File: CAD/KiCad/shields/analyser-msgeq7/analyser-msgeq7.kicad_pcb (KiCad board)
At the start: 2 copper layers, 150 x 55 mm, 59 parts, among them U1 MSGEQ7N, U2 MSGEQ7N, U3 MSGEQ7N, U4 MSGEQ7N, U5 MSGEQ7N

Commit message: Remove shield identification and adopt the simplified connector and Teensy pin maps
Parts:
- removed CID1: 100nF, Shields:C_0603_1608Metric
- removed JSID1: WRITE ENABLE - OPEN, Shields:SolderJumper-2_P1.3mm_Open_RoundedPad1.0x1.5mm
- removed RID1: 10K, Shields:R_0603_1608Metric
- removed UID1: M24C02-RMN6TP, Shields:SOIC-8_3.9x4.9mm_P1.27mm
- added TPG: AGND, Shields:TestPoint_Pad_D1.5mm, F.Cu at (183.0, 90.0)
- added TPI: IOREF, Shields:TestPoint_Pad_D1.5mm, F.Cu at (178.0, 90.0)
- JA1: value ANALYSER - KEY 24 -> ANALYSER - KEY 22; footprint Shields:Socket_2x12_Key24 -> Shields:Socket_2x11_Key22
- TP11: value test pad -> male1/analyser out
- TP12: value test pad -> male2/analyser out
- TP13: value test pad -> female1/analyser out
- TP14: value test pad -> female2/analyser out
- TP15: value test pad -> female3/analyser out
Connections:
- JA1 pad 19: shield/sda -> IOREF
- JA1 pad 20: shield/scl -> (no net)
- JA1 pad 21: IOREF -> (no net)
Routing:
- net GND: track 144.2 -> 0.00 mm, vias 2 -> 0
- net shield/scl: track 140.6 -> 0.00 mm, vias 1 -> 0
- net shield/sda: track 135.4 -> 0.00 mm, vias 2 -> 0
- net IOREF: track 217.2 -> 186.1 mm, vias 4 -> 3
- net AGND: track 345.4 -> 316.4 mm, vias 10 -> 12
- net female1/analyser out: track 26.0 -> 51.6 mm, vias 2 -> 3
- net id/wp: track 19.2 -> 0.00 mm, vias 2 -> 0
- net male2/microphone: track 148.9 -> 131.6 mm, vias 1 -> 2
- net male2/analyser out: track 124.9 -> 138.0 mm, vias 2 -> 3
- net analyser/reset: track 145.6 -> 157.3 mm, vias 7 -> 6
- net female2/microphone: track 56.3 -> 66.6 mm
- net female3/microphone: track 88.5 -> 81.4 mm, vias 1 -> 2
- net male1/microphone: track 106.9 -> 113.6 mm, vias 2 -> 1
- net analyser/strobe: track 158.1 -> 164.7 mm, vias 5 -> 7
- net female2/analyser out: track 52.8 -> 46.9 mm
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- removed copper zone on B.Cu, net AGND
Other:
- board text added: "1"
- board text added: "AGND"
- board text added: "ANA 0"
- board text added: "ANA 1"
- board text added: "ANA 2"
- board text added: "ANA 3"
- board text added: "ANA 4"
- board text added: "ANALYSER - 5 x MSGEQ7 - BANDS"
- board text added: "CH0 F1"
- board text added: "CH1 F2"
- board text added: "CH2 F3"
- board text added: "CH3 M1"
- board text added: "CH4 M2"
- board text added: "IOREF"
- board text added: "KEY <-"
- board text added: "OPEN UNLESS MEASURED"
- board text added: "REF - NEVER GROUND"
- board text added: "RESET"
- board text added: "STROBE"
- board text removed: "ANALYSER-MSGEQ7"

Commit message: Finish revised shield routing, printed identification and clean KiCad checks
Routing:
- added copper zone on B.Cu, net AGND
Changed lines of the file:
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@@
 		(descr "Physical top-view contact map; bottom mounted socket, blocked final cavity")
 		(property "Reference" "JA1"
-			(at 0 0 0)
+			(at 6 0 0)
 			(layer "F.SilkS")
 			(effects
@@
 			(size 1.7 1.7)
 			(drill 1)
-			(layers "*.Cu")
+			(layers "*.Cu" "*.Mask")
 			(remove_unused_layers no)
 			(net 8 "female1{slash}microphone")
@@
 			(size 1.7 1.7)
 			(drill 1)
-			(layers "*.Cu")
+			(layers "*.Cu" "*.Mask")
 			(remove_unused_layers no)
 			(net 1 "AGND")
@@
 			(size 1.7 1.7)
 			(drill 1)
-			(layers "*.Cu")
+			(layers "*.Cu" "*.Mask")
 			(remove_unused_layers no)
 			(net 14 "female2{slash}microphone")
@@
 			(size 1.7 1.7)
 			(drill 1)
-			(layers "*.Cu")
+			(layers "*.Cu" "*.Mask")
 			(remove_unused_layers no)
 			(net 1 "AGND")
@@
 			(size 1.7 1.7)
 			(drill 1)
-			(layers "*.Cu")
+			(layers "*.Cu" "*.Mask")
 			(remove_unused_layers no)
 			(net 20 "female3{slash}microphone")
@@
 			(size 1.7 1.7)
 			(drill 1)
-			(layers "*.Cu")
+			(layers "*.Cu" "*.Mask")
 			(remove_unused_layers no)
 			(net 1 "AGND")
@@
 			(size 1.7 1.7)
 			(drill 1)
-			(layers "*.Cu")
+			(layers "*.Cu" "*.Mask")
 			(remove_unused_layers no)
 			(net 26 "male1{slash}microphone")
@@
 			(size 1.7 1.7)
 			(drill 1)
-			(layers "*.Cu")
+			(layers "*.Cu" "*.Mask")
 			(remove_unused_layers no)
 			(net 1 "AGND")
@@
 			(size 1.7 1.7)
 			(drill 1)
-			(layers "*.Cu")
+			(layers "*.Cu" "*.Mask")
 			(remove_unused_layers no)
 			(net 32 "male2{slash}microphone")
@@
 			(size 1.7 1.7)
 			(drill 1)
-			(layers "*.Cu")
+			(layers "*.Cu" "*.Mask")
 			(remove_unused_layers no)
 			(net 1 "AGND")
@@
 			(size 1.7 1.7)
 			(drill 1)
-			(layers "*.Cu")
+			(layers "*.Cu" "*.Mask")
 			(remove_unused_layers no)
 			(net 5 "female1{slash}analyser out")
@@
 			(size 1.7 1.7)
 			(drill 1)
-			(layers "*.Cu")
+			(layers "*.Cu" "*.Mask")
 			(remove_unused_layers no)
 			(net 11 "female2{slash}analyser out")
@@
 			(size 1.7 1.7)
 			(drill 1)
-			(layers "*.Cu")
+			(layers "*.Cu" "*.Mask")
 			(remove_unused_layers no)
 			(net 17 "female3{slash}analyser out")
@@
 			(size 1.7 1.7)
 			(drill 1)
-			(layers "*.Cu")
+			(layers "*.Cu" "*.Mask")
 			(remove_unused_layers no)
 			(net 23 "male1{slash}analyser out")
@@
 			(size 1.7 1.7)
 			(drill 1)
-			(layers "*.Cu")
+			(layers "*.Cu" "*.Mask")
 			(remove_unused_layers no)
 			(net 29 "male2{slash}analyser out")
@@
 			(size 1.7 1.7)
 			(drill 1)
-			(layers "*.Cu")
+			(layers "*.Cu" "*.Mask")
 			(remove_unused_layers no)
 			(net 1 "AGND")
@@
 			(size 1.7 1.7)
 			(drill 1)
-			(layers "*.Cu")
+			(layers "*.Cu" "*.Mask")
 			(remove_unused_layers no)
 			(net 4 "analyser{slash}strobe")
@@
 			(size 1.7 1.7)
 			(drill 1)
-			(layers "*.Cu")
+			(layers "*.Cu" "*.Mask")
 			(remove_unused_layers no)
 			(net 3 "analyser{slash}reset")
@@
 			(size 1.7 1.7)
 			(drill 1)
-			(layers "*.Cu")
+			(layers "*.Cu" "*.Mask")
 			(remove_unused_layers no)
 			(net 2 "IOREF")
@@
 			(size 1.7 1.7)
 			(drill 1)
-			(layers "*.Cu")
+			(layers "*.Cu" "*.Mask")
 			(remove_unused_layers no)
 			(thermal_bridge_angle 45)
@@
 			(size 1.7 1.7)
 			(drill 1)
-			(layers "*.Cu")
+			(layers "*.Cu" "*.Mask")
 			(remove_unused_layers no)
 			(thermal_bridge_angle 45)
@@
 		(layer "Edge.Cuts")
 	)
-	(gr_text "ANALYSER - 5 x MSGEQ7 - BANDS"
-		(at 123 52 0)
-		(layer "F.SilkS")
-		(effects
-			(font
-				(size 1.2 1.2)
-				(thickness 0.12)
-			)
-		)
-	)
 	(gr_text "CH1 F2"
 		(at 93 59 0)
@@
 		)
 	)
-	(gr_text "IOREF"
-		(at 178 92 0)
+	(gr_text "OPEN UNLESS\nMEASURED"
+		(at 69 91 0)
 		(layer "F.SilkS")
 		(effects
@@
 		)
 	)
-	(gr_text "ANA 0"
-		(at 62 76 0)
+	(gr_text "REF - NEVER\nGROUND"
+		(at 104 76 0)
 		(layer "F.SilkS")
 		(effects
@@
 		)
 	)
-	(gr_text "ANA 2"
-		(at 110 76 0)
+	(gr_text "ANA 4"
+		(at 158 76 0)
 		(layer "F.SilkS")
 		(effects
@@
 		)
 	)
-	(gr_text "CH0 F1"
-		(at 69 59 0)
+	(gr_text "CH3 M1"
+		(at 141 59 0)
 		(layer "F.SilkS")
 		(effects
@@
 		)
 	)
-	(gr_text "ANA 1"
-		(at 86 76 0)
+	(gr_text "OPEN UNLESS\nMEASURED"
+		(at 165 91 0)
 		(layer "F.SilkS")
 		(effects
@@
 		)
 	)
-	(gr_text "RESET"
-		(at 190 58 0)
+	(gr_text "OPEN UNLESS\nMEASURED"
+		(at 93 91 0)
 		(layer "F.SilkS")
 		(effects
@@
 		)
 	)
-	(gr_text "REF - NEVER\nGROUND"
-		(at 102.5 76 0)
+	(gr_text "ANA 2"
+		(at 111.5 76 0)
 		(layer "F.SilkS")
 		(effects
@@
 		)
 	)
-	(gr_text "ANA 4"
-		(at 158 76 0)
+	(gr_text "REF - NEVER\nGROUND"
+		(at 176 76 0)
 		(layer "F.SilkS")
 		(effects
@@
 		)
 	)
-	(gr_text "OPEN UNLESS\nMEASURED"
-		(at 141 91 0)
+	(gr_text "ANA 3"
+		(at 134 76 0)
 		(layer "F.SilkS")
 		(effects
@@
 		)
 	)
-	(gr_text "AGND"
-		(at 183 92 0)
+	(gr_text "ANALYSER - 5 x MSGEQ7 - BANDS"
+		(at 123 52 0)
 		(layer "F.SilkS")
 		(effects
 			(font
-				(size 0.8 0.8)
+				(size 1.2 1.2)
 				(thickness 0.12)
 			)
 		)
 	)
-	(gr_text "CH2 F3"
-		(at 117 59 0)
+	(gr_text "REF - NEVER\nGROUND"
+		(at 80 76 0)
 		(layer "F.SilkS")
 		(effects
 			(font
-				(size 0.9 0.9)
+				(size 0.8 0.8)
 				(thickness 0.12)
 			)
 		)
 	)
-	(gr_text "KEY <-"
-		(at 60 79.4 0)
+	(gr_text "1"
+		(at 52 52 0)
 		(layer "F.SilkS")
 		(effects
@@
 		)
 	)
-	(gr_text "REF - NEVER\nGROUND"
-		(at 78.5 76 0)
+	(gr_text "ANA 1"
+		(at 87.5 76 0)
 		(layer "F.SilkS")
 		(effects
@@
 		)
 	)
-	(gr_text "OPEN UNLESS\nMEASURED"
-		(at 93 91 0)
+	(gr_text "STROBE"
+		(at 180 58 0)
 		(layer "F.SilkS")
 		(effects
@@
 		)
 	)
-	(gr_text "1"
-		(at 52 52 0)
+	(gr_text "KEY <-"
+		(at 60 79.4 0)
 		(layer "F.SilkS")
 		(effects
@@
 		)
 	)
-	(gr_text "CH4 M2"
-		(at 165 59 0)
+	(gr_text "ANA 0"
+		(at 62 76 0)
 		(layer "F.SilkS")
 		(effects
 			(font
-				(size 0.9 0.9)
+				(size 0.8 0.8)
 				(thickness 0.12)
 			)
 		)
 	)
-	(gr_text "STROBE"
-		(at 180 58 0)
+	(gr_text "REF - NEVER\nGROUND"
+		(at 150.5 76 0)
 		(layer "F.SilkS")
 		(effects
@@
 		)
 	)
-	(gr_text "ANA 3"
-		(at 134 76 0)
+	(gr_text "CH0 F1"
+		(at 69 59 0)
 		(layer "F.SilkS")
 		(effects
 			(font
-				(size 0.8 0.8)
+				(size 0.9 0.9)
 				(thickness 0.12)
 			)
 		)
 	)
-	(gr_text "REF - NEVER\nGROUND"
-		(at 176 76 0)
+	(gr_text "IOREF"
+		(at 178 92 0)
 		(layer "F.SilkS")
 		(effects
@@
 		)
 	)
-	(gr_text "REF - NEVER\nGROUND"
-		(at 150.5 76 0)
+	(gr_text "AGND"
+		(at 183 92 0)
 		(layer "F.SilkS")
 		(effects
@@
 		)
 	)
-	(gr_text "CH3 M1"
-		(at 141 59 0)
+	(gr_text "CH2 F3"
+		(at 117 59 0)
 		(layer "F.SilkS")
 		(effects
@@
 	)
 	(gr_text "OPEN UNLESS\nMEASURED"
-		(at 69 91 0)
+		(at 141 91 0)
 		(layer "F.SilkS")
 		(effects
@@
 		)
 	)
-	(gr_text "OPEN UNLESS\nMEASURED"
-		(at 165 91 0)
+	(gr_text "REF - NEVER\nGROUND"
+		(at 126.5 76 0)
 		(layer "F.SilkS")
 		(effects
@@
 		)
 	)
-	(gr_text "REF - NEVER\nGROUND"
-		(at 126.5 76 0)
+	(gr_text "RESET"
+		(at 190 58 0)
 		(layer "F.SilkS")
 		(effects
@@
 		)
 	)
+	(gr_text "CH4 M2"
+		(at 165 59 0)
+		(layer "F.SilkS")
+		(effects
+			(font
+				(size 0.9 0.9)
+				(thickness 0.12)
+			)
+		)
+	)
 	(segment
 		(start 133.3322 64.365)
@@
 		(net 34)
 	)
+	(zone
+		(net 1)
+		(net_name "AGND")
+		(layer "B.Cu")
+		(name "SH_RETURN")
+		(hatch edge 0.5)
+		(connect_pads yes
+			(clearance 0.25)
+		)
+		(min_thickness 0.2)
+		(filled_areas_thickness no)
+		(fill yes
+			(thermal_gap 0.5)
+			(thermal_bridge_width 0.5)
+		)
+		(polygon
+			(pts
+				(xy 50.45 50.45) (xy 199.55 50.45) (xy 199.55 104.55) (xy 50.45 104.55)
+			)
+		)
+	)
 	(embedded_fonts no)

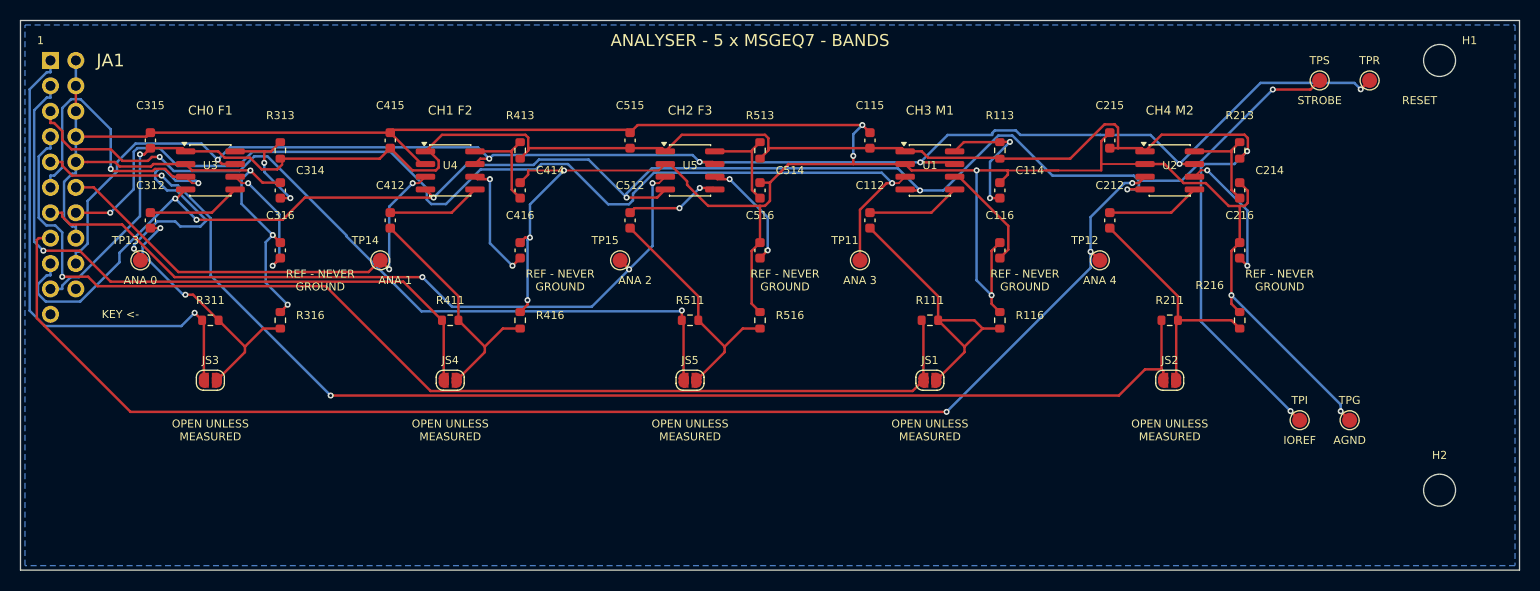
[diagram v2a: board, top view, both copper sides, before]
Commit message: Route microphones directly to Teensy and remove the analyser buffer board
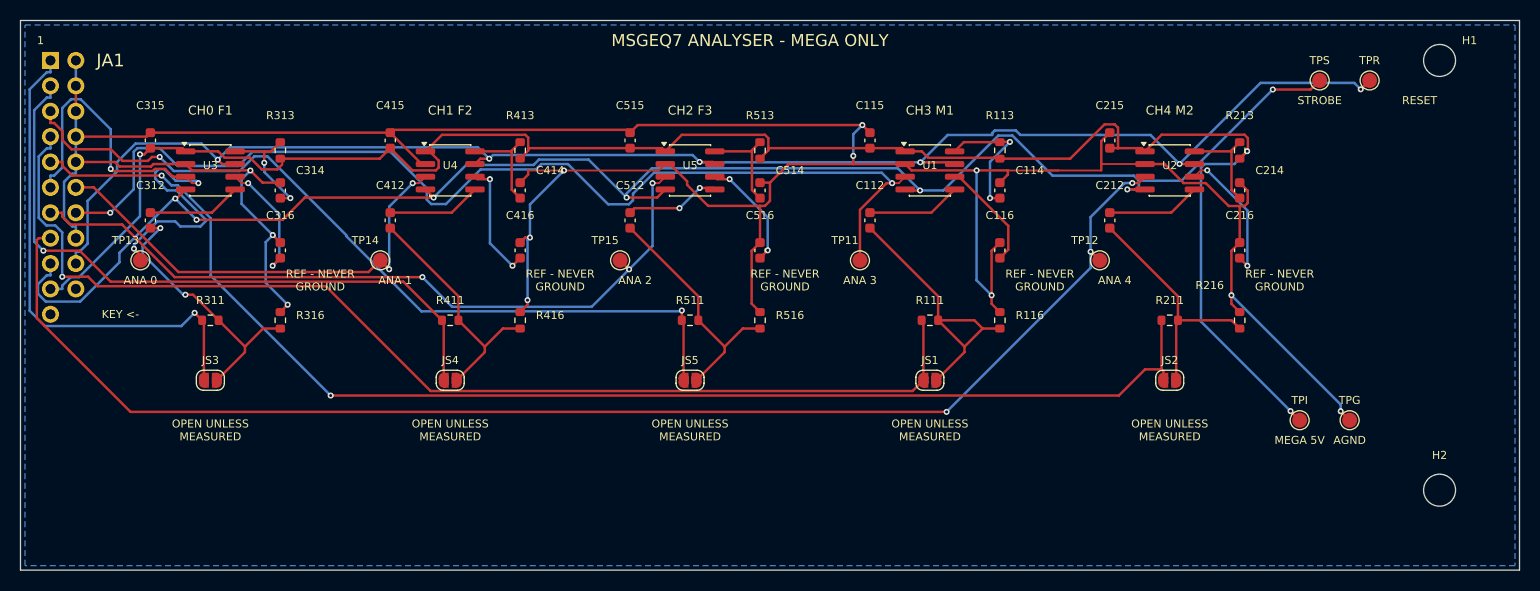
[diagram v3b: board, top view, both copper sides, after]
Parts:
- TPI: value IOREF -> MEGA_5V
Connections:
- net IOREF renamed MEGA_5V
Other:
- board text added: "MEGA 5V"
- board text added: "MSGEQ7 ANALYSER - MEGA ONLY"
- board text removed: "ANALYSER - 5 x MSGEQ7 - BANDS"
- board text removed: "IOREF"
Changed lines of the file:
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@@
 	(net 0 "")
 	(net 1 "AGND")
-	(net 2 "IOREF")
+	(net 2 "MEGA_5V")
 	(net 3 "analyser{slash}reset")
 	(net 4 "analyser{slash}strobe")
@@
 			)
 		)
-		(property "Value" "IOREF"
+		(property "Value" "MEGA_5V"
 			(at 0 1.75 0)
 			(layer "F.Fab")
@@
 			(size 1.5 1.5)
 			(layers "F.Cu" "F.Mask")
-			(net 2 "IOREF")
+			(net 2 "MEGA_5V")
 		)
 		(embedded_fonts no)
@@
 			(layers "F.Cu" "F.Mask" "F.Paste")
 			(roundrect_rratio 0.25)
-			(net 2 "IOREF")
+			(net 2 "MEGA_5V")
 		)
 		(pad "2" smd roundrect
@@
 			(layers "F.Cu" "F.Mask" "F.Paste")
 			(roundrect_rratio 0.25)
-			(net 2 "IOREF")
+			(net 2 "MEGA_5V")
 		)
 		(pad "2" smd roundrect
@@
 			(layers "F.Cu" "F.Mask" "F.Paste")
 			(roundrect_rratio 0.25)
-			(net 2 "IOREF")
+			(net 2 "MEGA_5V")
 		)
 		(pad "2" smd roundrect
@@
 			(layers "F.Cu" "F.Mask" "F.Paste")
 			(roundrect_rratio 0.25)
-			(net 2 "IOREF")
+			(net 2 "MEGA_5V")
 		)
 		(pad "2" smd roundrect
@@
 			(layers "F.Cu" "F.Mask" "F.Paste")
 			(roundrect_rratio 0.25)
-			(net 2 "IOREF")
+			(net 2 "MEGA_5V")
 		)
 		(pad "2" smd roundrect
@@
 			(layers "F.Cu" "F.Mask" "F.Paste")
 			(roundrect_rratio 0.25)
-			(net 2 "IOREF")
+			(net 2 "MEGA_5V")
 		)
 		(pad "2" smd roundrect
@@
 			(layers "F.Cu" "F.Mask" "F.Paste")
 			(roundrect_rratio 0.25)
-			(net 2 "IOREF")
+			(net 2 "MEGA_5V")
 		)
 		(pad "2" smd roundrect
@@
 			(layers "F.Cu" "F.Mask" "F.Paste")
 			(roundrect_rratio 0.25)
-			(net 2 "IOREF")
+			(net 2 "MEGA_5V")
 		)
 		(pad "2" smd roundrect
@@
 			(layers "F.Cu" "F.Mask" "F.Paste")
 			(roundrect_rratio 0.25)
-			(net 2 "IOREF")
+			(net 2 "MEGA_5V")
 		)
 		(pad "2" smd roundrect
@@
 			(layers "F.Cu" "F.Mask" "F.Paste")
 			(roundrect_rratio 0.25)
-			(net 2 "IOREF")
+			(net 2 "MEGA_5V")
 		)
 		(pad "2" smd roundrect
@@
 			(layers "F.Cu" "F.Mask" "F.Paste")
 			(roundrect_rratio 0.25)
-			(net 2 "IOREF")
+			(net 2 "MEGA_5V")
 		)
 		(pad "2" smd roundrect
@@
 			(layers "F.Cu" "F.Mask" "F.Paste")
 			(roundrect_rratio 0.25)
-			(net 2 "IOREF")
+			(net 2 "MEGA_5V")
 		)
 		(pad "2" smd roundrect
@@
 			(layers "F.Cu" "F.Mask" "F.Paste")
 			(roundrect_rratio 0.25)
-			(net 2 "IOREF")
+			(net 2 "MEGA_5V")
 		)
 		(pad "2" smd roundrect
@@
 			(layers "F.Cu" "F.Mask" "F.Paste")
 			(roundrect_rratio 0.25)
-			(net 2 "IOREF")
+			(net 2 "MEGA_5V")
 		)
 		(pad "2" smd roundrect
@@
 			(layers "F.Cu" "F.Mask" "F.Paste")
 			(roundrect_rratio 0.25)
-			(net 2 "IOREF")
+			(net 2 "MEGA_5V")
 		)
 		(pad "2" smd roundrect
@@
 			(layers "*.Cu" "*.Mask")
 			(remove_unused_layers no)
-			(net 2 "IOREF")
+			(net 2 "MEGA_5V")
 			(thermal_bridge_angle 45)
 		)
@@
 		(layer "Edge.Cuts")
 	)
-	(gr_text "CH1 F2"
-		(at 93 59 0)
+	(gr_text "1"
+		(at 52 52 0)
 		(layer "F.SilkS")
 		(effects
 			(font
-				(size 0.9 0.9)
+				(size 0.8 0.8)
 				(thickness 0.12)
 			)
 		)
 	)
-	(gr_text "OPEN UNLESS\nMEASURED"
-		(at 69 91 0)
+	(gr_text "REF - NEVER\nGROUND"
+		(at 80 76 0)
 		(layer "F.SilkS")
 		(effects
@@
 	)
 	(gr_text "REF - NEVER\nGROUND"
-		(at 104 76 0)
+		(at 152 76 0)
 		(layer "F.SilkS")
 		(effects
@@
 		)
 	)
-	(gr_text "ANA 4"
-		(at 158 76 0)
+	(gr_text "ANA 1"
+		(at 87.5 76 0)
 		(layer "F.SilkS")
 		(effects
@@
 		)
 	)
-	(gr_text "OPEN UNLESS\nMEASURED"
-		(at 117 91 0)
+	(gr_text "MSGEQ7 ANALYSER - MEGA ONLY"
+		(at 123 52 0)
 		(layer "F.SilkS")
 		(effects
 			(font
-				(size 0.8 0.8)
+				(size 1.2 1.2)
 				(thickness 0.12)
 			)
 		)
 	)
-	(gr_text "CH3 M1"
-		(at 141 59 0)
+	(gr_text "AGND"
+		(at 183 92 0)
 		(layer "F.SilkS")
 		(effects
 			(font
-				(size 0.9 0.9)
+				(size 0.8 0.8)
 				(thickness 0.12)
 			)
 		)
 	)
-	(gr_text "OPEN UNLESS\nMEASURED"
-		(at 165 91 0)
+	(gr_text "CH0 F1"
+		(at 69 59 0)
 		(layer "F.SilkS")
 		(effects
 			(font
-				(size 0.8 0.8)
+				(size 0.9 0.9)
 				(thickness 0.12)
 			)
@@
 	)
 	(gr_text "OPEN UNLESS\nMEASURED"
-		(at 93 91 0)
+		(at 165 91 0)
 		(layer "F.SilkS")
 		(effects
@@
 		)
 	)
-	(gr_text "ANA 2"
-		(at 111.5 76 0)
+	(gr_text "OPEN UNLESS\nMEASURED"
+		(at 141 91 0)
 		(layer "F.SilkS")
 		(effects
@@
 		)
 	)
-	(gr_text "REF - NEVER\nGROUND"
-		(at 176 76 0)
+	(gr_text "CH4 M2"
+		(at 165 59 0)
 		(layer "F.SilkS")
 		(effects
 			(font
-				(size 0.8 0.8)
+				(size 0.9 0.9)
 				(thickness 0.12)
 			)
 		)
 	)
-	(gr_text "ANA 3"
-		(at 134 76 0)
+	(gr_text "CH3 M1"
+		(at 141 59 0)
 		(layer "F.SilkS")
 		(effects
 			(font
-				(size 0.8 0.8)
+				(size 0.9 0.9)
 				(thickness 0.12)
 			)
 		)
 	)
-	(gr_text "ANALYSER - 5 x MSGEQ7 - BANDS"
-		(at 123 52 0)
+	(gr_text "REF - NEVER\nGROUND"
+		(at 104 76 0)
 		(layer "F.SilkS")
 		(effects
 			(font
-				(size 1.2 1.2)
+				(size 0.8 0.8)
 				(thickness 0.12)
 			)
 		)
 	)
-	(gr_text "REF - NEVER\nGROUND"
-		(at 80 76 0)
+	(gr_text "OPEN UNLESS\nMEASURED"
+		(at 93 91 0)
 		(layer "F.SilkS")
 		(effects
@@
 		)
 	)
-	(gr_text "1"
-		(at 52 52 0)
+	(gr_text "CH2 F3"
+		(at 117 59 0)
 		(layer "F.SilkS")
 		(effects
 			(font
-				(size 0.8 0.8)
+				(size 0.9 0.9)
 				(thickness 0.12)
 			)
 		)
 	)
-	(gr_text "ANA 1"
-		(at 87.5 76 0)
+	(gr_text "OPEN UNLESS\nMEASURED"
+		(at 117 91 0)
 		(layer "F.SilkS")
 		(effects
@@
 		)
 	)
-	(gr_text "STROBE"
-		(at 180 58 0)
+	(gr_text "OPEN UNLESS\nMEASURED"
+		(at 69 91 0)
 		(layer "F.SilkS")
 		(effects
@@
 		)
 	)
-	(gr_text "KEY <-"
-		(at 60 79.4 0)
+	(gr_text "ANA 4"
+		(at 159.5 76 0)
 		(layer "F.SilkS")
 		(effects
@@
 		)
 	)
-	(gr_text "ANA 0"
-		(at 62 76 0)
+	(gr_text "ANA 3"
+		(at 134 76 0)
 		(layer "F.SilkS")
 		(effects
@@
 	)
 	(gr_text "REF - NEVER\nGROUND"
-		(at 150.5 76 0)
+		(at 126.5 76 0)
 		(layer "F.SilkS")
 		(effects
@@
 		)
 	)
-	(gr_text "CH0 F1"
-		(at 69 59 0)
+	(gr_text "ANA 2"
+		(at 111.5 76 0)
 		(layer "F.SilkS")
 		(effects
 			(font
-				(size 0.9 0.9)
+				(size 0.8 0.8)
 				(thickness 0.12)
 			)
 		)
 	)
-	(gr_text "IOREF"
-		(at 178 92 0)
+	(gr_text "REF - NEVER\nGROUND"
+		(at 176 76 0)
 		(layer "F.SilkS")
 		(effects
@@
 		)
 	)
-	(gr_text "AGND"
-		(at 183 92 0)
+	(gr_text "RESET"
+		(at 190 58 0)
 		(layer "F.SilkS")
 		(effects
@@
 		)
 	)
-	(gr_text "CH2 F3"
-		(at 117 59 0)
+	(gr_text "STROBE"
+		(at 180 58 0)
 		(layer "F.SilkS")
 		(effects
 			(font
-				(size 0.9 0.9)
+				(size 0.8 0.8)
 				(thickness 0.12)
 			)
 		)
 	)
-	(gr_text "OPEN UNLESS\nMEASURED"
-		(at 141 91 0)
+	(gr_text "KEY <-"
+		(at 60 79.4 0)
 		(layer "F.SilkS")
 		(effects
@@
 		)
 	)
-	(gr_text "REF - NEVER\nGROUND"
-		(at 126.5 76 0)
+	(gr_text "CH1 F2"
+		(at 93 59 0)
 		(layer "F.SilkS")
 		(effects
 			(font
-				(size 0.8 0.8)
+				(size 0.9 0.9)
 				(thickness 0.12)
 			)
 		)
 	)
-	(gr_text "RESET"
-		(at 190 58 0)
+	(gr_text "MEGA 5V"
+		(at 178 92 0)
 		(layer "F.SilkS")
 		(effects
@@
 		)
 	)
-	(gr_text "CH4 M2"
-		(at 165 59 0)
+	(gr_text "ANA 0"
+		(at 62 76 0)
 		(layer "F.SilkS")
 		(effects
 			(font
-				(size 0.9 0.9)
+				(size 0.8 0.8)
 				(thickness 0.12)
 			)
